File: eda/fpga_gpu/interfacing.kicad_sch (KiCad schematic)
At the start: 14 parts, among them U11 74HCT00, U3 74HCT541, U4 74HCT541, U5 74HCT541, U6 TXS0108EPW, U7 TXS0108EPW

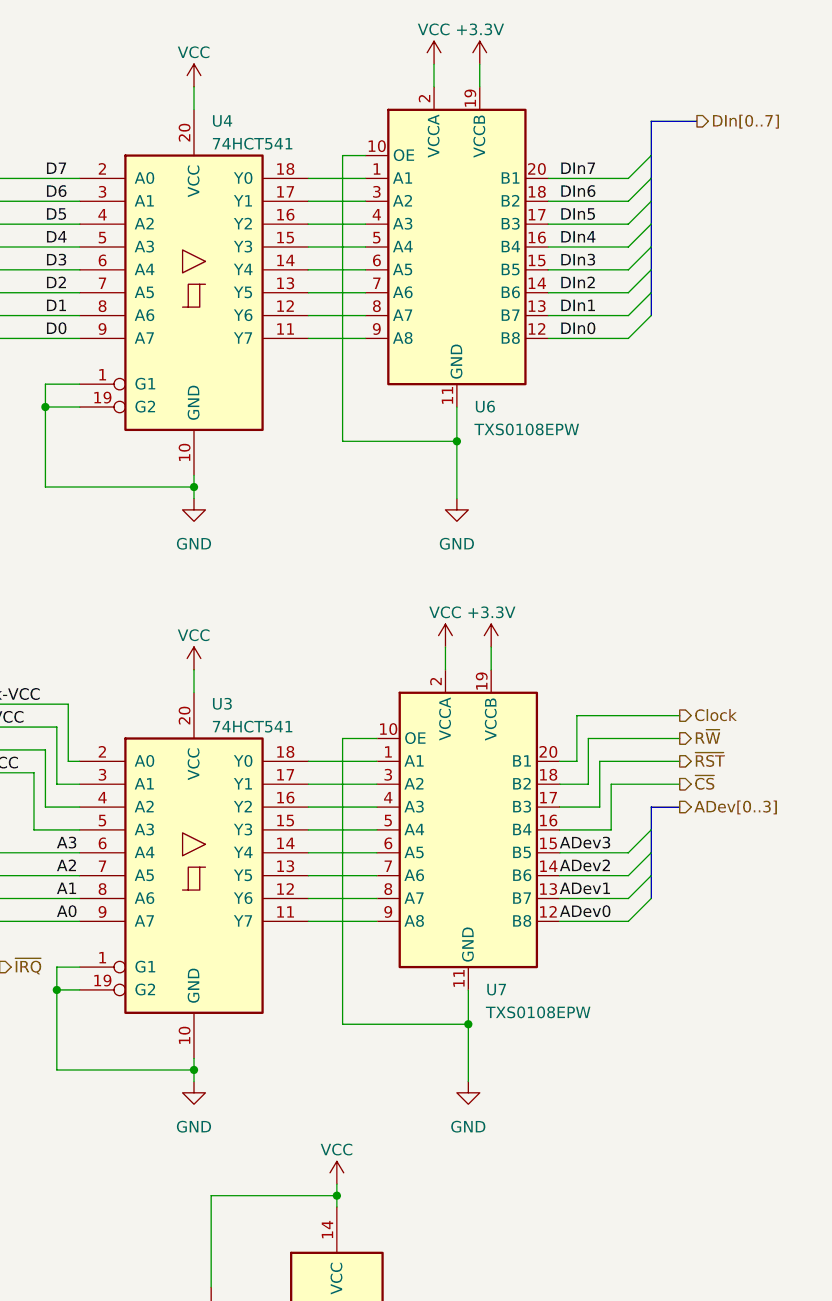
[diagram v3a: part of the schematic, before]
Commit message: Generate step files and start on gpu for new board layout
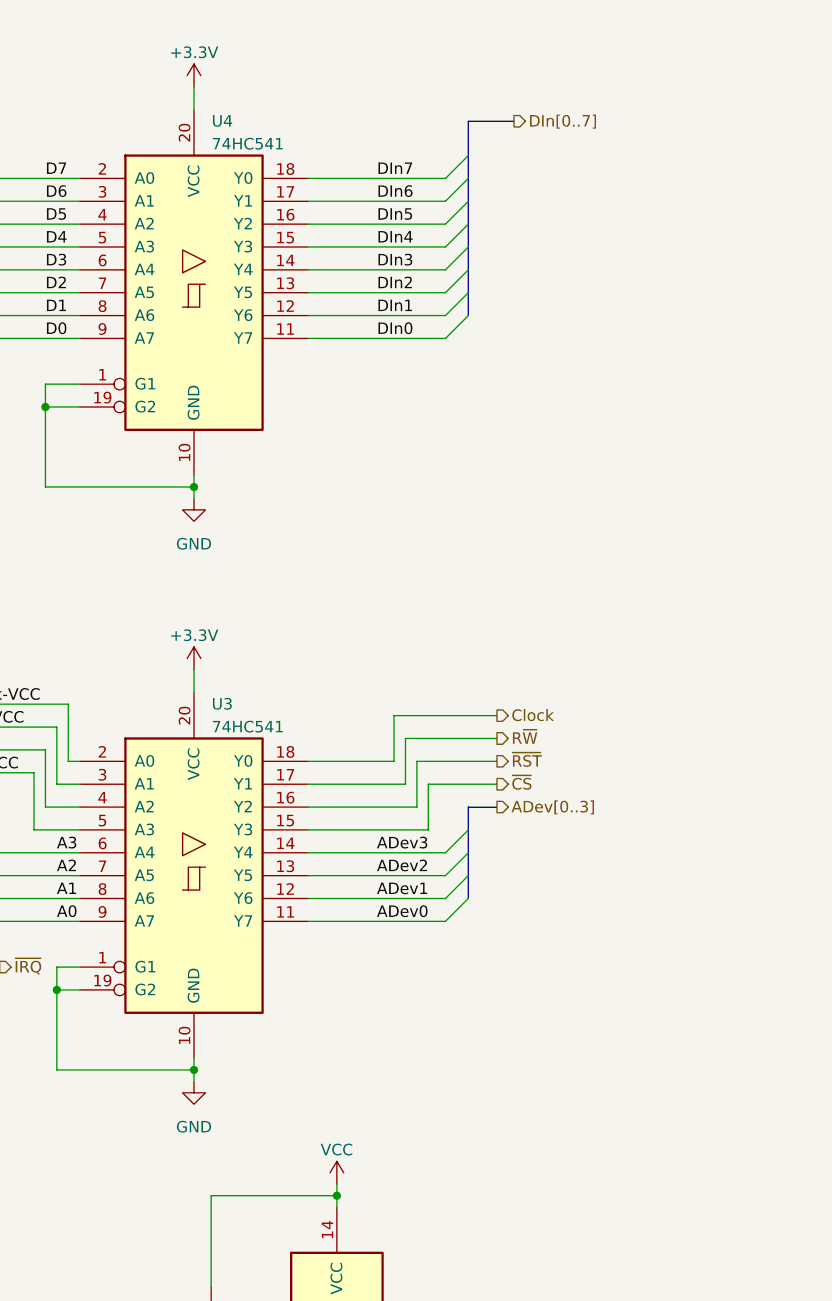
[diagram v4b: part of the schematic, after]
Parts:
- removed U6, U7: TXS0108EPW, Package_SO:TSSOP-20_4.4x6.5mm_P0.65mm, symbol Logic_LevelTranslator:TXS0108EPW
- U3, U4: value 74HCT541 -> 74HC541
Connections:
- net +3.3V: now also U3.20 (VCC), U4.20 (VCC)
- net ADev0: now also U3.11 (Y7)
- net ADev1: now also U3.12 (Y6)
- net ADev2: now also U3.13 (Y5)
- net ADev3: now also U3.14 (Y4)
- net Clock: now also U3.18 (Y0)
- net DIn0: now also U4.11 (Y7)
- net DIn1: now also U4.12 (Y6)
- net DIn2: now also U4.13 (Y5)
- net DIn3: now also U4.14 (Y4)
- net DIn4: now also U4.15 (Y3)
- net DIn5: now also U4.16 (Y2)
- net DIn6: now also U4.17 (Y1)
- net DIn7: now also U4.18 (Y0)
- net R~{W}: now also U3.17 (Y1)
- net VCC: no longer U3.20 (VCC), U4.20 (VCC)
- net ~{CS}: now also U3.15 (Y3)
- net ~{RST}: now also U3.16 (Y2)
